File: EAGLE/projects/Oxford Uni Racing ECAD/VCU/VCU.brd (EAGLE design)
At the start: 165.1 x 114 mm, 19 parts, among them J1 PWR_CAN, J3 MC_LEFT, J4 MC_RIGHT, X2 D-SUB9-H2M09ST

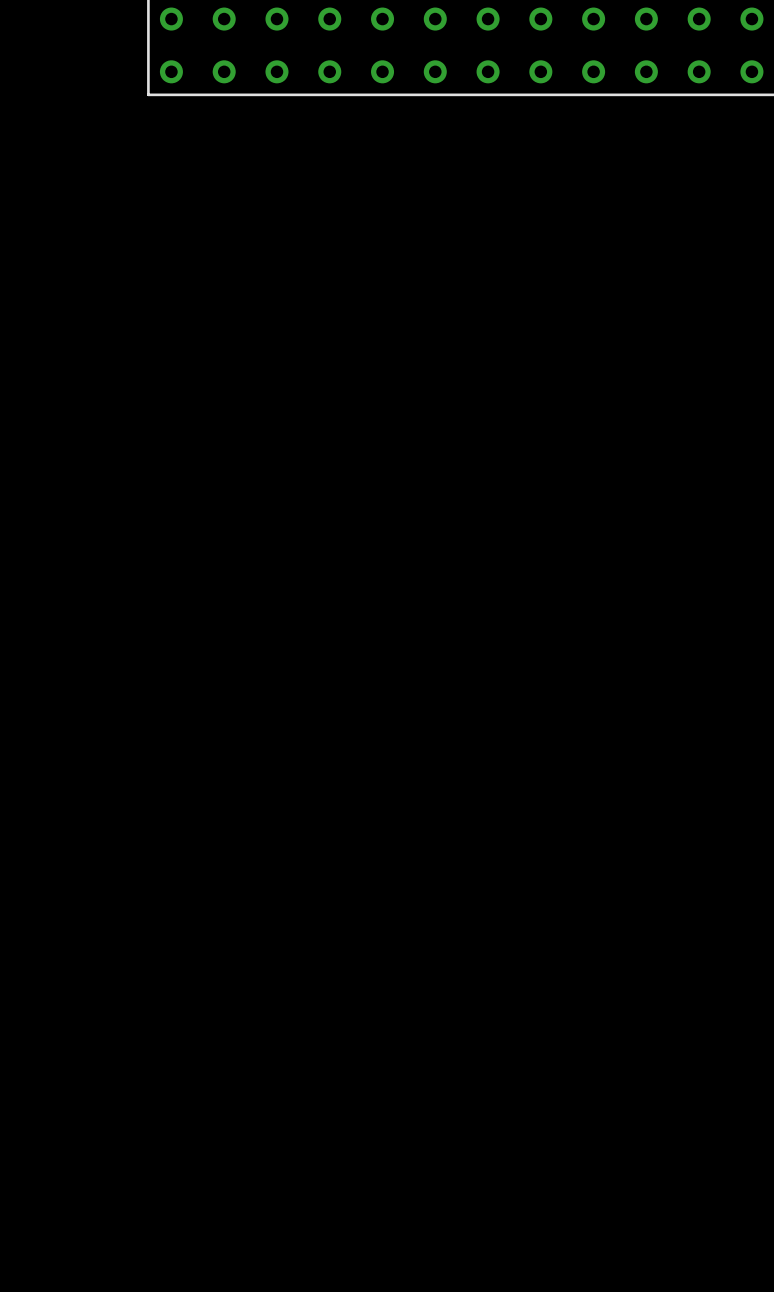
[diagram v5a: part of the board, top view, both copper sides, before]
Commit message: added microcontroller output to a connected to relay to ASS to VCU
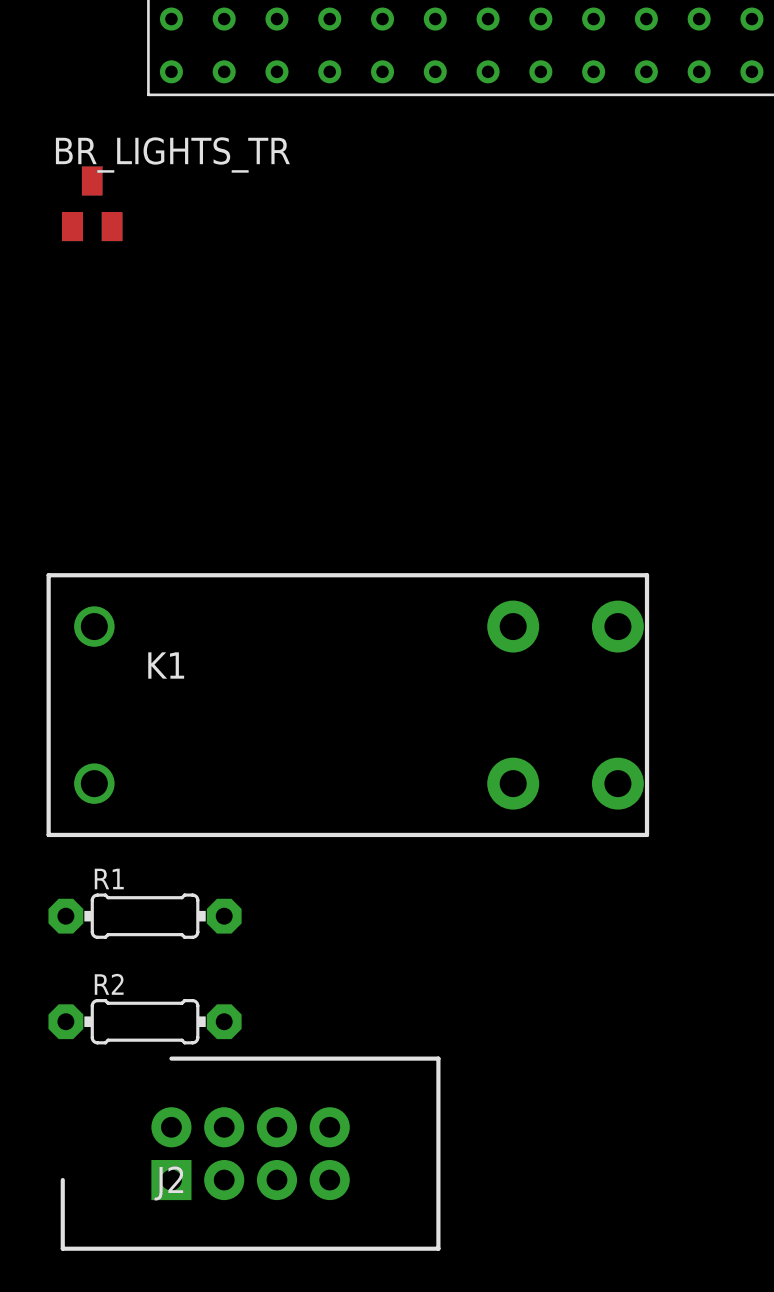
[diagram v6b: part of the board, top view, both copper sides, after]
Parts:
- added BR_LIGHTS_TR: IRLML2502GTRPBF, adafruit:SOT23
- added J2: PWR_CAN, T821108A1S100CEU:HDRV8W64P254_2X4_1778X895X915P
- added K1: RT444012, relay:RT2N/O
- added R1: 1K, adafruit:0204/7
- added R2: 47K, adafruit:0204/7
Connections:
- new net ASS1: J2.1, K1.14
- new net ASS2: J2.2, K1.11
- new net N$1: R1.1, U$1.J5031
- new net N$3: BR_LIGHTS_TR.1, R1.2, R2.2
- new net N$6: BR_LIGHTS_TR.3, K1.A2
- net 12V: now also K1.A1
- net GND: now also BR_LIGHTS_TR.2, R2.1
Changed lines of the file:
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@@
 <attribute name="VALUE" x="91.567" y="62.992" size="1.27" layer="27" ratio="10" rot="R90"/>
+</element>
+<element name="BR_LIGHTS_TR" library="adafruit" library_urn="urn:adsk.eagle:library:420" package="SOT23" package3d_urn="urn:adsk.eagle:package:6240836/1" value="IRLML2502GTRPBF" x="-48.26" y="-34.29" smashed="yes">
+<attribute name="NAME" x="-50.165" y="-32.385" size="1.27" layer="25"/>
+<attribute name="VALUE" x="-50.165" y="-37.465" size="1.27" layer="27"/>
+</element>
+<element name="K1" library="relay" library_urn="urn:adsk.eagle:library:339" package="RT2N/O" package3d_urn="urn:adsk.eagle:package:24520/1" value="RT444012" x="-35.56" y="-58.42" smashed="yes">
+<attribute name="MF" value="" x="-35.56" y="-58.42" size="1.778" layer="27" display="off"/>
+<attribute name="MPN" value="" x="-35.56" y="-58.42" size="1.778" layer="27" display="off"/>
+<attribute name="NAME" x="-45.72" y="-57.15" size="1.27" layer="25"/>
+<attribute name="OC_FARNELL" value="unknown" x="-35.56" y="-58.42" size="1.778" layer="27" display="off"/>
+<attribute name="OC_NEWARK" value="unknown" x="-35.56" y="-58.42" size="1.778" layer="27" display="off"/>
+<attribute name="VALUE" x="-45.72" y="-59.69" size="1.27" layer="27"/>
+</element>
+<element name="R1" library="adafruit" library_urn="urn:adsk.eagle:library:420" package="0204/7" package3d_urn="urn:adsk.eagle:package:6240596/1" value="1K" x="-45.72" y="-68.58" smashed="yes">
+<attribute name="NAME" x="-48.26" y="-67.2846" size="0.9906" layer="25" ratio="12"/>
+<attribute name="VALUE" x="-47.3456" y="-69.0626" size="0.9906" layer="27" ratio="12"/>
+</element>
+<element name="R2" library="adafruit" library_urn="urn:adsk.eagle:library:420" package="0204/7" package3d_urn="urn:adsk.eagle:package:6240596/1" value="47K" x="-45.72" y="-73.66" smashed="yes">
+<attribute name="NAME" x="-48.26" y="-72.3646" size="0.9906" layer="25" ratio="12"/>
+<attribute name="VALUE" x="-47.3456" y="-74.1426" size="0.9906" layer="27" ratio="12"/>
+</element>
+<element name="J2" library="T821108A1S100CEU" package="HDRV8W64P254_2X4_1778X895X915P" value="PWR_CAN" x="-44.45" y="-81.28" smashed="yes">
+<attribute name="DESCRIPTION" value="HEADER, VERTICAL, 2.54MM, 8WAY Amphenol T821 Series, 2.54mm Pitch 8 Way 2 Row Straight PCB Header, Solder Termination, 3A" x="-44.45" y="-81.28" size="1.778" layer="27" display="off"/>
+<attribute name="HEIGHT" value="9.15mm" x="-44.45" y="-81.28" size="1.778" layer="27" display="off"/>
+<attribute name="MANUFACTURER_NAME" value="Amphenol" x="-44.45" y="-81.28" size="1.778" layer="27" display="off"/>
+<attribute name="MANUFACTURER_PART_NUMBER" value="T821108A1S100CEU" x="-44.45" y="-81.28" size="1.778" layer="27" display="off"/>
+<attribute name="NAME" x="-44.45" y="-81.28" size="1.27" layer="25" align="center"/>
+<attribute name="RS_PART_NUMBER" value="1702738" x="-44.45" y="-81.28" size="1.778" layer="27" display="off"/>
+<attribute name="VALUE" x="-44.45" y="-81.28" size="1.27" layer="27" align="center"/>
 </element>
 </elements>
@@
 <wire x1="93.98" y1="64.77" x2="95.25" y2="63.5" width="0.4064" layer="1"/>
 <wire x1="95.25" y1="63.5" x2="95.25" y2="59.69" width="0.4064" layer="1"/>
+<contactref element="BR_LIGHTS_TR" pad="2"/>
+<contactref element="R2" pad="1"/>
 <wire x1="96.52" y1="22.86" x2="95.25" y2="59.69" width="0" layer="19" extent="1-1"/>
 <wire x1="110.49" y1="10.16" x2="100.33" y2="11.43" width="0" layer="19" extent="16-16"/>
@@
 <wire x1="12.7" y1="-24.13" x2="17.78" y2="-24.13" width="0" layer="19" extent="1-1"/>
 <wire x1="10.16" y1="-26.67" x2="12.7" y2="-24.13" width="0" layer="19" extent="1-1"/>
+<wire x1="-47.31" y1="-35.39" x2="10.16" y2="-26.67" width="0" layer="19" extent="1-1"/>
+<wire x1="-49.53" y1="-73.66" x2="-47.31" y2="-35.39" width="0" layer="19" extent="1-1"/>
 </signal>
 <signal name="CANL">
@@
 <wire x1="139.7" y1="7.62" x2="134.62" y2="7.62" width="1.27" layer="16"/>
 <wire x1="134.62" y1="7.62" x2="130.81" y2="7.62" width="1.27" layer="16"/>
+<contactref element="K1" pad="A1"/>
 <wire x1="119.38" y1="7.62" x2="130.81" y2="7.62" width="0" layer="19" extent="16-16"/>
 <wire x1="99.06" y1="20.32" x2="110.49" y2="7.62" width="0" layer="19" extent="16-16"/>
+<wire x1="-48.16" y1="-62.2" x2="99.06" y2="20.32" width="0" layer="19" extent="1-1"/>
 </signal>
 <signal name="N$2">
@@
 <wire x1="-1.27" y1="5.08" x2="92.71" y2="62.23" width="0" layer="19" extent="1-1"/>
 </signal>
+<signal name="N$1">
+<contactref element="U$1" pad="J5031"/>
+<contactref element="R1" pad="1"/>
+<wire x1="-1.27" y1="20.32" x2="-49.53" y2="-68.58" width="0" layer="19" extent="1-1"/>
+</signal>
+<signal name="N$3">
+<contactref element="R1" pad="2"/>
+<contactref element="BR_LIGHTS_TR" pad="1"/>
+<contactref element="R2" pad="2"/>
+<wire x1="-41.91" y1="-68.58" x2="-41.91" y2="-73.66" width="0" layer="19" extent="1-1"/>
+<wire x1="-49.21" y1="-35.39" x2="-41.91" y2="-68.58" width="0" layer="19" extent="1-1"/>
+</signal>
+<signal name="N$6">
+<contactref element="K1" pad="A2"/>
+<contactref element="BR_LIGHTS_TR" pad="3"/>
+<wire x1="-48.26" y1="-33.19" x2="-48.16" y2="-54.64" width="0" layer="19" extent="1-1"/>
+</signal>
+<signal name="ASS1">
+<contactref element="K1" pad="14"/>
+<contactref element="J2" pad="1"/>
+<wire x1="-22.96" y1="-62.2" x2="-44.45" y2="-81.28" width="0" layer="19" extent="1-1"/>
+</signal>
+<signal name="ASS2">
+<contactref element="K1" pad="11"/>
+<contactref element="J2" pad="2"/>
+<wire x1="-28" y1="-62.2" x2="-44.45" y2="-78.74" width="0" layer="19" extent="1-1"/>
+</signal>
 </signals>

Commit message: fixed can wiring on VCU
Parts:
- J2: value PWR_CAN -> ASS
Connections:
- net RXD: now also U$1.J5046; no longer U$1.J5037
- net TXD: now also U$1.J5047; no longer U$1.J5036
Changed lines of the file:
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@@
 <attribute name="VALUE" x="-47.3456" y="-74.1426" size="0.9906" layer="27" ratio="12"/>
 </element>
-<element name="J2" library="T821108A1S100CEU" package="HDRV8W64P254_2X4_1778X895X915P" value="PWR_CAN" x="-44.45" y="-81.28" smashed="yes">
+<element name="J2" library="T821108A1S100CEU" package="HDRV8W64P254_2X4_1778X895X915P" value="ASS" x="-44.45" y="-81.28" smashed="yes">
 <attribute name="DESCRIPTION" value="HEADER, VERTICAL, 2.54MM, 8WAY Amphenol T821 Series, 2.54mm Pitch 8 Way 2 Row Straight PCB Header, Solder Termination, 3A" x="-44.45" y="-81.28" size="1.778" layer="27" display="off"/>
 <attribute name="HEIGHT" value="9.15mm" x="-44.45" y="-81.28" size="1.778" layer="27" display="off"/>
@@
 <signal name="TXD">
 <contactref element="U$3" pad="PIN_0"/>
-<contactref element="U$1" pad="J5036"/>
-<wire x1="-1.27" y1="7.62" x2="92.71" y2="66.04" width="0" layer="19" extent="1-1"/>
+<contactref element="U$1" pad="J5047"/>
+<wire x1="-49.53" y1="-22.86" x2="92.71" y2="66.04" width="0" layer="19" extent="1-1"/>
 </signal>
 <signal name="RXD">
 <contactref element="U$3" pad="PIN_3"/>
-<contactref element="U$1" pad="J5037"/>
-<wire x1="-1.27" y1="5.08" x2="92.71" y2="62.23" width="0" layer="19" extent="1-1"/>
+<contactref element="U$1" pad="J5046"/>
+<wire x1="-49.53" y1="-20.32" x2="92.71" y2="62.23" width="0" layer="19" extent="1-1"/>
 </signal>
 <signal name="N$1">

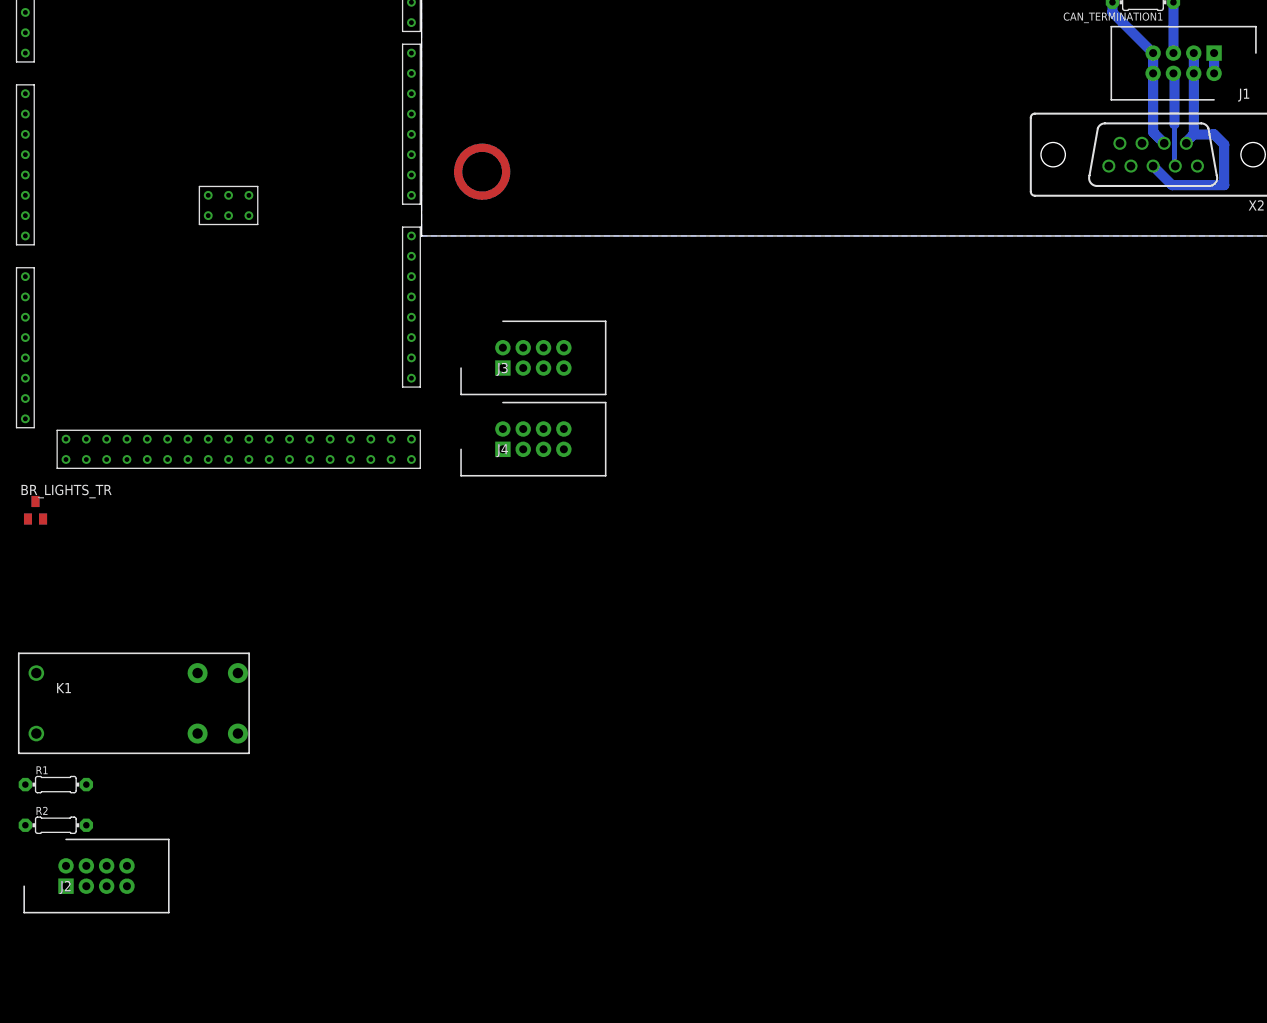
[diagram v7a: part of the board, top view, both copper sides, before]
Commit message: added fuses to boards
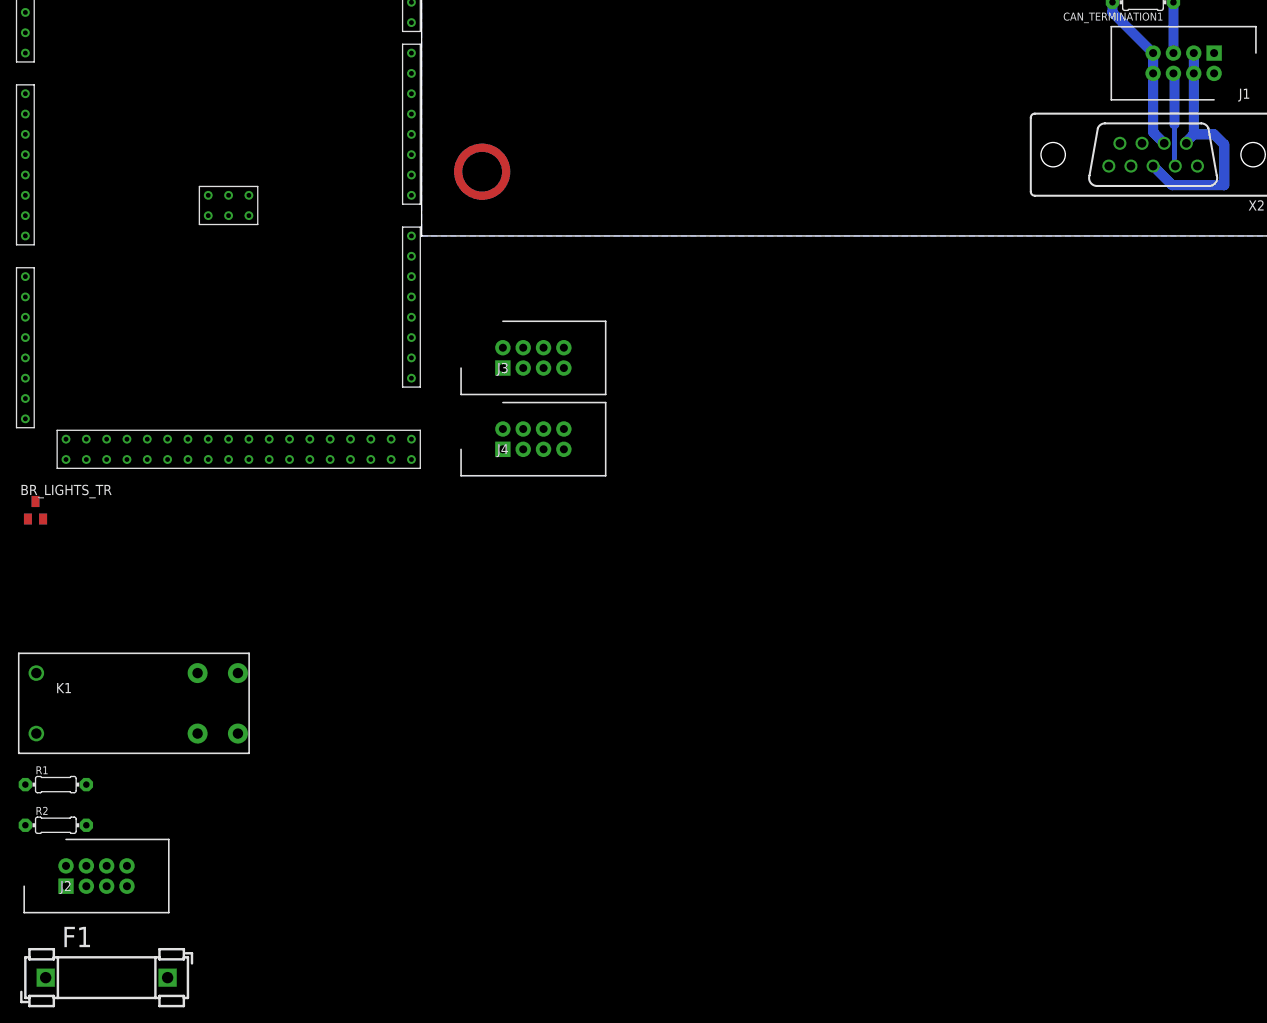
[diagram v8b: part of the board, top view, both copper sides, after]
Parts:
- added F1: 1A, fuse:FUSE_HOLDER_5X20MM
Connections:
- new net 12V_BATTERY: F1.1, J1.1, J1.2
- net 12V: now also F1.2; no longer J1.1, J1.2
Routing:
- net 12V: track 20.3 -> 17.8 mm
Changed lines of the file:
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@@
 <attribute name="VALUE" x="-44.45" y="-81.28" size="1.27" layer="27" align="center"/>
+</element>
+<element name="F1" library="fuse" library_urn="urn:adsk.eagle:library:233" package="FUSE_HOLDER_5X20MM" package3d_urn="urn:adsk.eagle:package:14079/1" value="1A" x="-46.99" y="-92.71" smashed="yes">
+<attribute name="MF" value="" x="-46.99" y="-92.71" size="1.778" layer="27" display="off"/>
+<attribute name="MPN" value="" x="-46.99" y="-92.71" size="1.778" layer="27" display="off"/>
+<attribute name="NAME" x="-44.958" y="-88.9" size="2.54" layer="25"/>
+<attribute name="OC_FARNELL" value="unknown" x="-46.99" y="-92.71" size="1.778" layer="27" display="off"/>
+<attribute name="OC_NEWARK" value="unknown" x="-46.99" y="-92.71" size="1.778" layer="27" display="off"/>
+<attribute name="VALUE" x="-45.212" y="-98.552" size="2.54" layer="27"/>
 </element>
 </elements>
@@
 </signal>
 <signal name="12V">
-<contactref element="J1" pad="1"/>
-<contactref element="J1" pad="2"/>
-<wire x1="99.06" y1="20.32" x2="99.06" y2="22.86" width="1.27" layer="16"/>
 <contactref element="IC2" pad="3"/>
 <contactref element="C3" pad="1"/>
@@
 <wire x1="134.62" y1="7.62" x2="130.81" y2="7.62" width="1.27" layer="16"/>
 <contactref element="K1" pad="A1"/>
+<contactref element="F1" pad="2"/>
 <wire x1="119.38" y1="7.62" x2="130.81" y2="7.62" width="0" layer="19" extent="16-16"/>
-<wire x1="99.06" y1="20.32" x2="110.49" y2="7.62" width="0" layer="19" extent="16-16"/>
-<wire x1="-48.16" y1="-62.2" x2="99.06" y2="20.32" width="0" layer="19" extent="1-1"/>
+<wire x1="-48.16" y1="-62.2" x2="110.49" y2="7.62" width="0" layer="19" extent="16-16"/>
+<wire x1="-31.75" y1="-92.71" x2="-48.16" y2="-62.2" width="0" layer="19" extent="1-1"/>
 </signal>
 <signal name="N$2">
@@
 <wire x1="-28" y1="-62.2" x2="-44.45" y2="-78.74" width="0" layer="19" extent="1-1"/>
 </signal>
+<signal name="12V_BATTERY">
+<contactref element="J1" pad="1"/>
+<contactref element="J1" pad="2"/>
+<contactref element="F1" pad="1"/>
+<wire x1="99.06" y1="20.32" x2="-46.99" y2="-92.71" width="0" layer="19" extent="1-1"/>
+<wire x1="99.06" y1="22.86" x2="99.06" y2="20.32" width="0" layer="19" extent="1-1"/>
+</signal>
 </signals>
